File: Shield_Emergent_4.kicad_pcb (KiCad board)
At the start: 4 copper layers, 27 x 36 mm, 37 parts, among them J1 TF31-18S-0.5SH_800_, J2 Conn_01x04_Socket, J3 TF31-18S-0.5SH_800_, J4 Conn_01x05, J5 Conn_01x02_Socket, J6 Conn_01x02_Socket, J7 Conn_01x05, J8 Conn_02x05_Odd_Even, U3 SP3012-06UTG, U4 SP3012-06UTG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

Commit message: v0.2 Draft routing
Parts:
- J8: footprint Connector_PinHeader_1.27mm:PinHeader_2x05_P1.27mm_Vertical -> myLib8:DS1020-04-10BVT1
- moved J8 4.42 mm to (13.9, 25.9), turned to 180 degrees
- moved U6 2.21 mm to (8.22, 22.9)
- moved R11 0.44 mm to (22.0, 12.0)
- moved R12 0.41 mm to (22.4, 27.8)
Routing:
- net K1: track 7.90 -> 11.5 mm
- net K3: track 6.58 -> 9.33 mm
- net K5: track 6.98 -> 9.32 mm
- net K4: track 10.5 -> 11.9 mm
- net K7: track 6.08 -> 7.30 mm
- net K9: track 6.25 -> 7.45 mm
- net K2: track 13.5 -> 14.6 mm
- net VBUS: track 72.8 -> 71.7 mm
- net 1_D+: track 12.1 -> 13.0 mm
- net K6: track 9.05 -> 9.69 mm
- net 2_D-: track 5.10 -> 5.68 mm
- net GND: vias 129 -> 137

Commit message: v0.3 actual state
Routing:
- net VBUS: track 71.7 -> 71.0 mm
- net GND: vias 137 -> 148

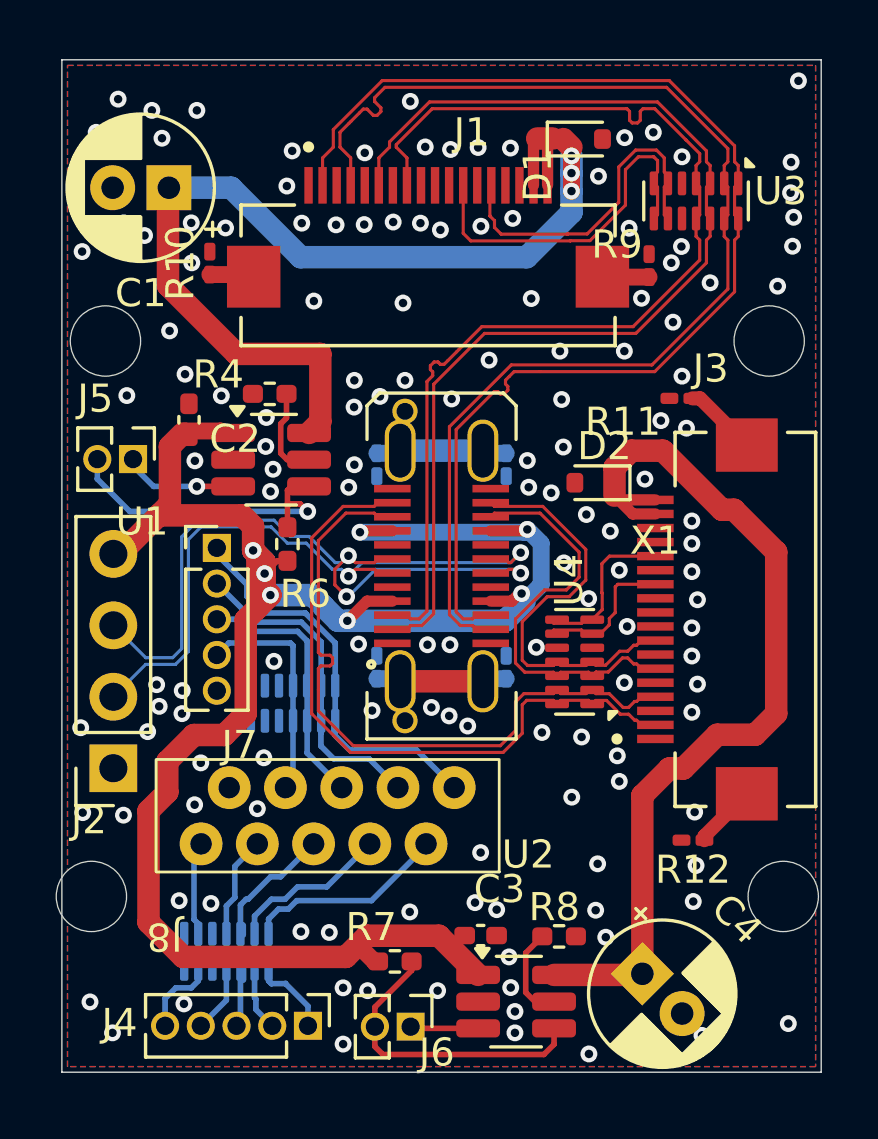
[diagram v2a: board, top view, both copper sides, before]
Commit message: v0.4  sent to Rezonit 4 the 1st time
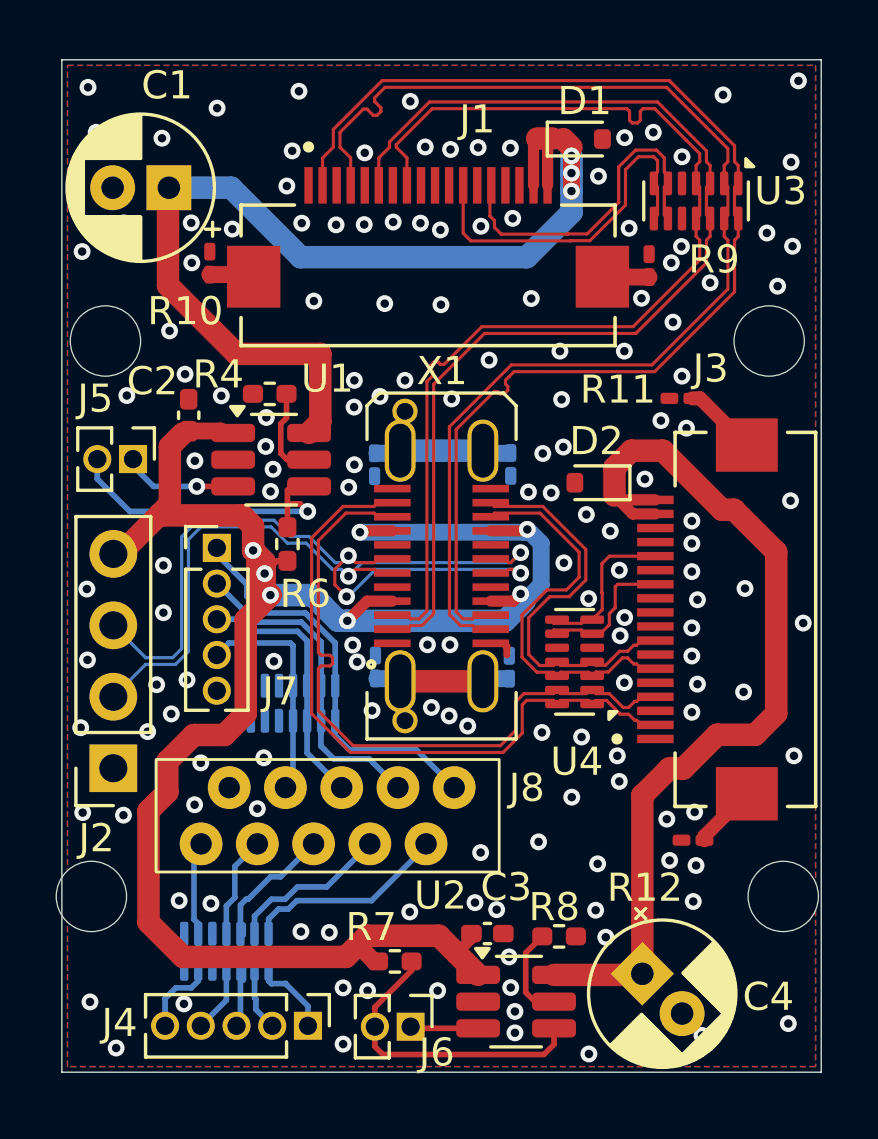
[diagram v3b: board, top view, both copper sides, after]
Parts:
- moved C3 0.25 mm to (15.1, 31.1)
- moved C2 0.16 mm to (4.51, 12.6)
- moved R1 0.16 mm to (16.0, 14.4)
- moved R2 0.11 mm to (15.9, 21.6)
- moved R3 0.08 mm to (11.1, 14.4)
- moved R5 0.05 mm to (11.2, 21.6)
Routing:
- net GND: track 0.00 -> 1.03 mm, vias 148 -> 160
- net VBUS: track 71.0 -> 71.9 mm
